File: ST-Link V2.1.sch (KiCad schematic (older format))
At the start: 3 parts

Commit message: drawing schematic
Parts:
- removed U?: stm32, symbol stm32
- added C10, C3: 1uF, symbol C
- added C15, C17, C18, C2, C5, C8, C9: 100nF, symbol C
- added C4: 10nF, symbol C
- added C6, C7: 20pF, symbol C
- added D? (x2): D, symbol D
- added J?: Conn_01x06, symbol Conn_01x06
- added LD1: LED_Dual_ACAC, symbol LED_Dual_ACAC
- added LD2: LED,RED, symbol LED
- added R1: 0, symbol R
- added R11, R2, R3: 100, symbol R
- added R14, R31: 100K, symbol R
- added R15: 4K7, symbol R
- added R16: 2K7, symbol R
- added R24: 10K, symbol R
- added R28: [NA], symbol R
- added R33, R34, R35: 22, symbol R
- added R4: 1K, symbol R
- added U2: LD3985M33R_SOT23, TO_SOT_Packages_SMD:SOT-23-5, symbol LD3985M33R_SOT23
- added U?: stm32, symbol stm32
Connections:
- net labels added: 3V3_ST_LINK, AIN_1, LED_STLINK, PWR_ENn, PWR_EXT, STLINK_RX, STM_JTCK, STM_JTMS, SWIM, SWIM_IN, SWIM_RST, SWIM_RST_IN, T_JTCK, T_JTMS, T_NRST, T_SWDIO_IN, T_SWO, USB_DM, USB_DP, USB_RENUMn, undone
- net labels removed: +3V3
- wire segments 23 -> 141
- no-connect marks 9 -> 12

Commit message: continue schematic
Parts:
- added C16: 20pF, symbol C
- added R22: 100, symbol R
- added R29, R30: 4K7, symbol R
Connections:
- net labels added: 3V3_ST_LINK1, AIN1, STLINK_TX
- wire segments 141 -> 148
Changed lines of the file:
@@
 Text GLabel 1300 2600 1    60   Input ~ 0
-undone
-Text GLabel 1800 2050 1    60   Input ~ 0
 undone
 $Comp
@@
 	800  3150 800  3600
 Wire Wire Line
-	800  3600 1750 3600
-Wire Wire Line
 	1750 3600 1750 3450
-Wire Wire Line
-	1450 3450 2600 3450
 Wire Wire Line
 	2550 3350 1450 3350
@@
 Connection ~ 1750 3450
 Connection ~ 1450 3350
-Text GLabel 1450 3300 1    60   Input ~ 0
-undone
 NoConn ~ 2550 3550
 Wire Wire Line
@@
 	7750 3900 7750 4000
 Connection ~ 8600 3900
+Wire Wire Line
+	4650 3250 5450 3250
+$Comp
+L R R22
+U 1 1 59D3403D
+P 5600 3250
+F 0 "R22" V 5680 3250 50  0000 C CNN
+F 1 "100" V 5600 3250 50  0000 C CNN
+F 2 "" V 5530 3250 50  0001 C CNN
+F 3 "" H 5600 3250 50  0001 C CNN
+	1    5600 3250
+	0    1    1    0
+$EndComp
+Wire Wire Line
+	5750 3250 6050 3250
+$Comp
+L C C16
+U 1 1 59D34298
+P 5850 3500
+F 0 "C16" H 5875 3600 50  0000 L CNN
+F 1 "20pF" H 5875 3400 50  0000 L CNN
+F 2 "" H 5888 3350 50  0001 C CNN
+F 3 "" H 5850 3500 50  0001 C CNN
+	1    5850 3500
+	1    0    0    -1
+$EndComp
+Wire Wire Line
+	5850 3250 5850 3350
+Connection ~ 5850 3250
+$Comp
+L GNDREF #PWR?
+U 1 1 59D34548
+P 5850 3650
+F 0 "#PWR?" H 5850 3400 50  0001 C CNN
+F 1 "GNDREF" H 5850 3500 50  0000 C CNN
+F 2 "" H 5850 3650 50  0001 C CNN
+F 3 "" H 5850 3650 50  0001 C CNN
+	1    5850 3650
+	1    0    0    -1
+$EndComp
+Wire Wire Line
+	950  2400 950  2500
+Text Label 950  2500 2    60   ~ 0
+3V3_ST_LINK1
+Wire Wire Line
+	1000 3550 1000 3700
+Connection ~ 1000 3600
+Wire Wire Line
+	1400 3300 1500 3300
+Text Label 1450 3300 0    60   ~ 0
+3V3_ST_LINK1
+$Comp
+L R R30
+U 1 1 59D3CD64
+P 1600 3450
+F 0 "R30" V 1680 3450 50  0000 C CNN
+F 1 "4K7" V 1600 3450 50  0000 C CNN
+F 2 "" V 1530 3450 50  0001 C CNN
+F 3 "" H 1600 3450 50  0001 C CNN
+	1    1600 3450
+	0    1    1    0
+$EndComp
+$Comp
+L R R29
+U 1 1 59D3CE9B
+P 1500 3600
+F 0 "R29" V 1580 3600 50  0000 C CNN
+F 1 "4K7" V 1500 3600 50  0000 C CNN
+F 2 "" V 1430 3600 50  0001 C CNN
+F 3 "" H 1500 3600 50  0001 C CNN
+	1    1500 3600
+	0    1    1    0
+$EndComp
+Wire Wire Line
+	1650 3600 1750 3600
+Wire Wire Line
+	800  3600 1350 3600
+Wire Wire Line
+	1750 3450 2550 3450
+Text Label 2350 3450 0    60   ~ 0
+AIN1
+Text Label 2400 4000 1    60   ~ 0
+STLINK_TX
+$Comp
+L GNDREF #PWR?
+U 1 1 59D3E32B
+P 1000 3700
+F 0 "#PWR?" H 1000 3450 50  0001 C CNN
+F 1 "GNDREF" H 1000 3550 50  0000 C CNN
+F 2 "" H 1000 3700 50  0001 C CNN
+F 3 "" H 1000 3700 50  0001 C CNN
+	1    1000 3700
+	1    0    0    -1
+$EndComp
 $EndSCHEMATC

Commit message: left usb and power part schematic
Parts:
- added J?: Conn_02x08_Row_Letter_First, symbol Conn_02x08_Row_Letter_First
- added JP2: Conn_02x01, symbol Conn_02x01
- added R13, R14: 47, symbol R
- added R8, R9: 220, symbol R
- added X1: 8MHz, symbol Crystal
- gave numbers to parts that had none: 1
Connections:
- net labels added: 5V_IN, RESET, ST_LINK_SWIM
- wire segments 148 -> 159
- no-connect marks 12 -> 14
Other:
- moved on the sheet: D?, R24, R28, R33, R34, R35

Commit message: still the same
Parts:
- added C? (x4): 1uF, symbol C
- added J?: USB_OTG, symbol USB_OTG
- added R?: R, symbol R
- added U?: MIC5219-3.3, TO_SOT_Packages_SMD:SOT-23-5, symbol MIC5219-3.3
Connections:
- wire segments 159 -> 176

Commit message: questions
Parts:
- removed D?: D, symbol D
- removed J?: Conn_01x06, symbol Conn_01x06
- removed R24: 10K, symbol R
- removed R28: [NA], symbol R
- removed R33, R34, R35: 22, symbol R
- added R10: 100, symbol R
- added R23: 36K, symbol R
- added R5: 100K, symbol R
- added R7, R8: 20, symbol R
- added R9: 10K, symbol R
- R6: renamed from R?; value R -> 1K5
- gave numbers to parts that had none: 8
- renumbered R14 to R19, R8 to R20, R9 to R21
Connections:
- net labels added: USB_RENUMN
- net labels removed: 3V3_ST_LINK1, AIN_1, T_JTMS, undone
- wire segments 176 -> 167
- no-connect marks 14 -> 13
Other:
- moved on the sheet: C15, C17, C5, C8, LD1, LD2, R1, R15, R2, R3, R4

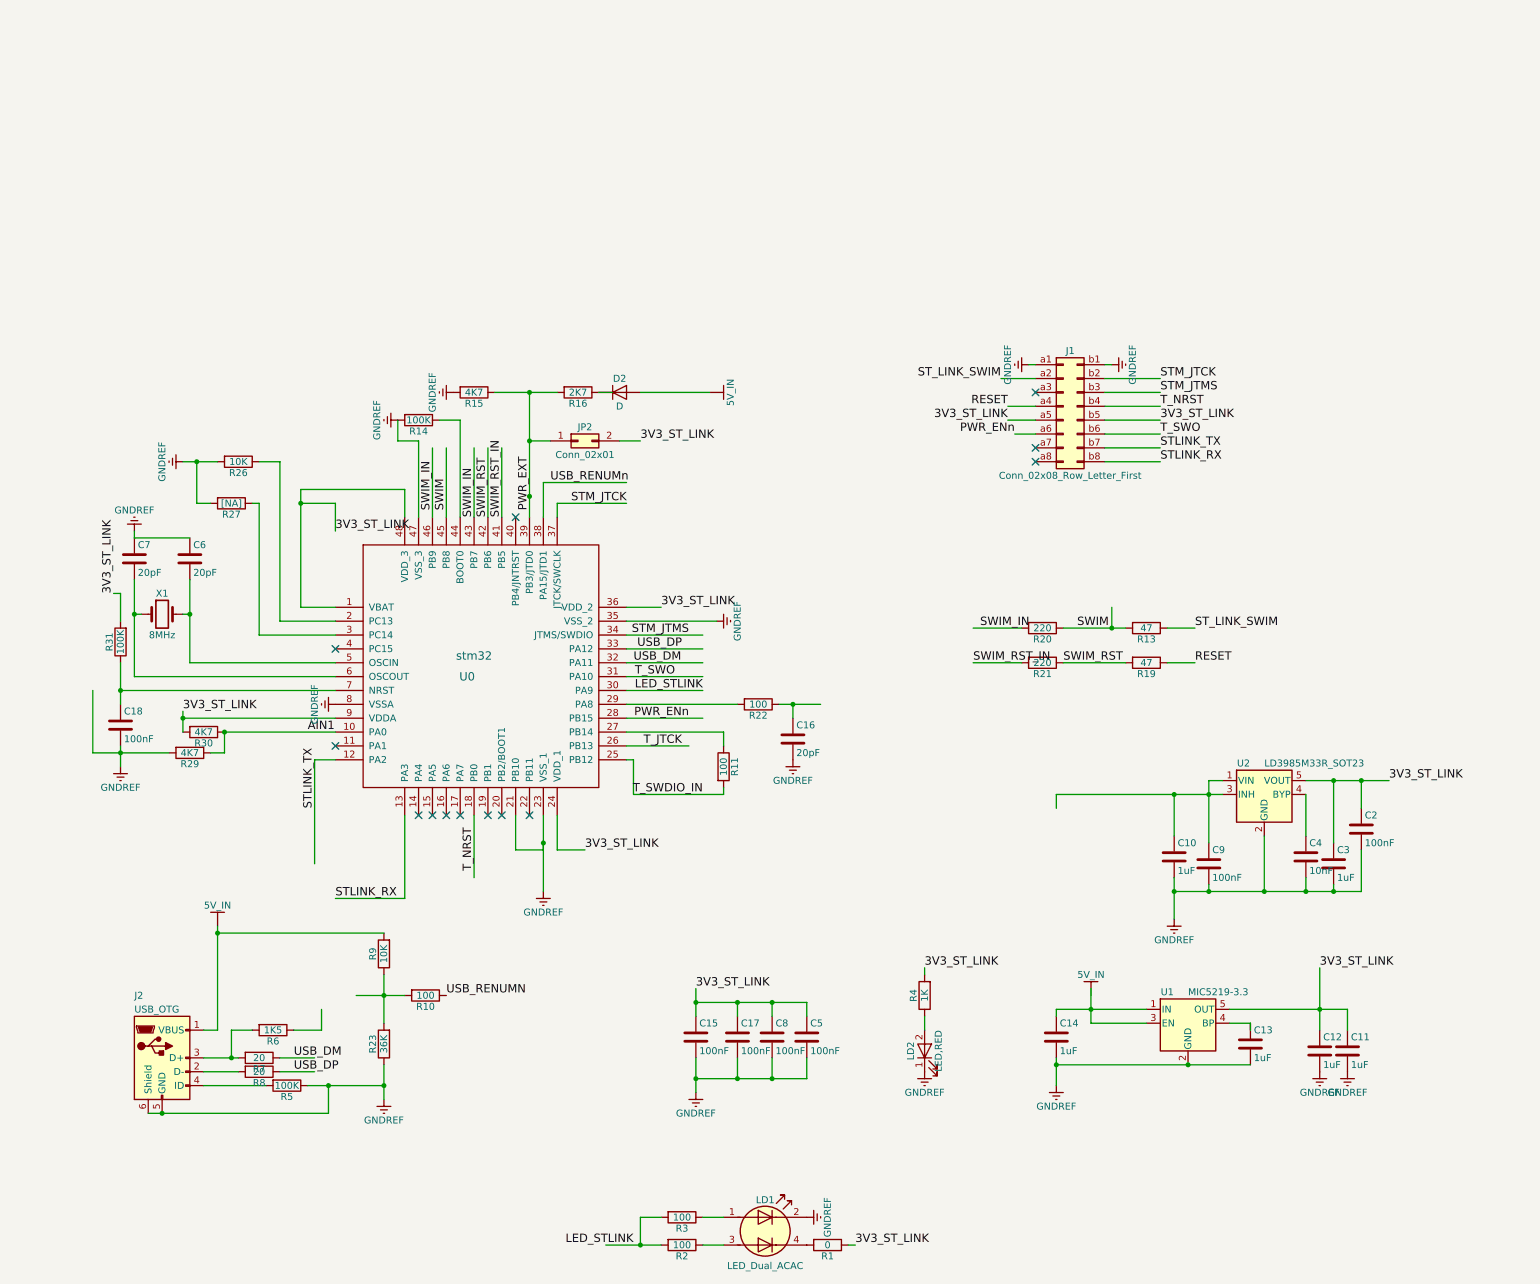
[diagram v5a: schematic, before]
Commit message: can start footprint
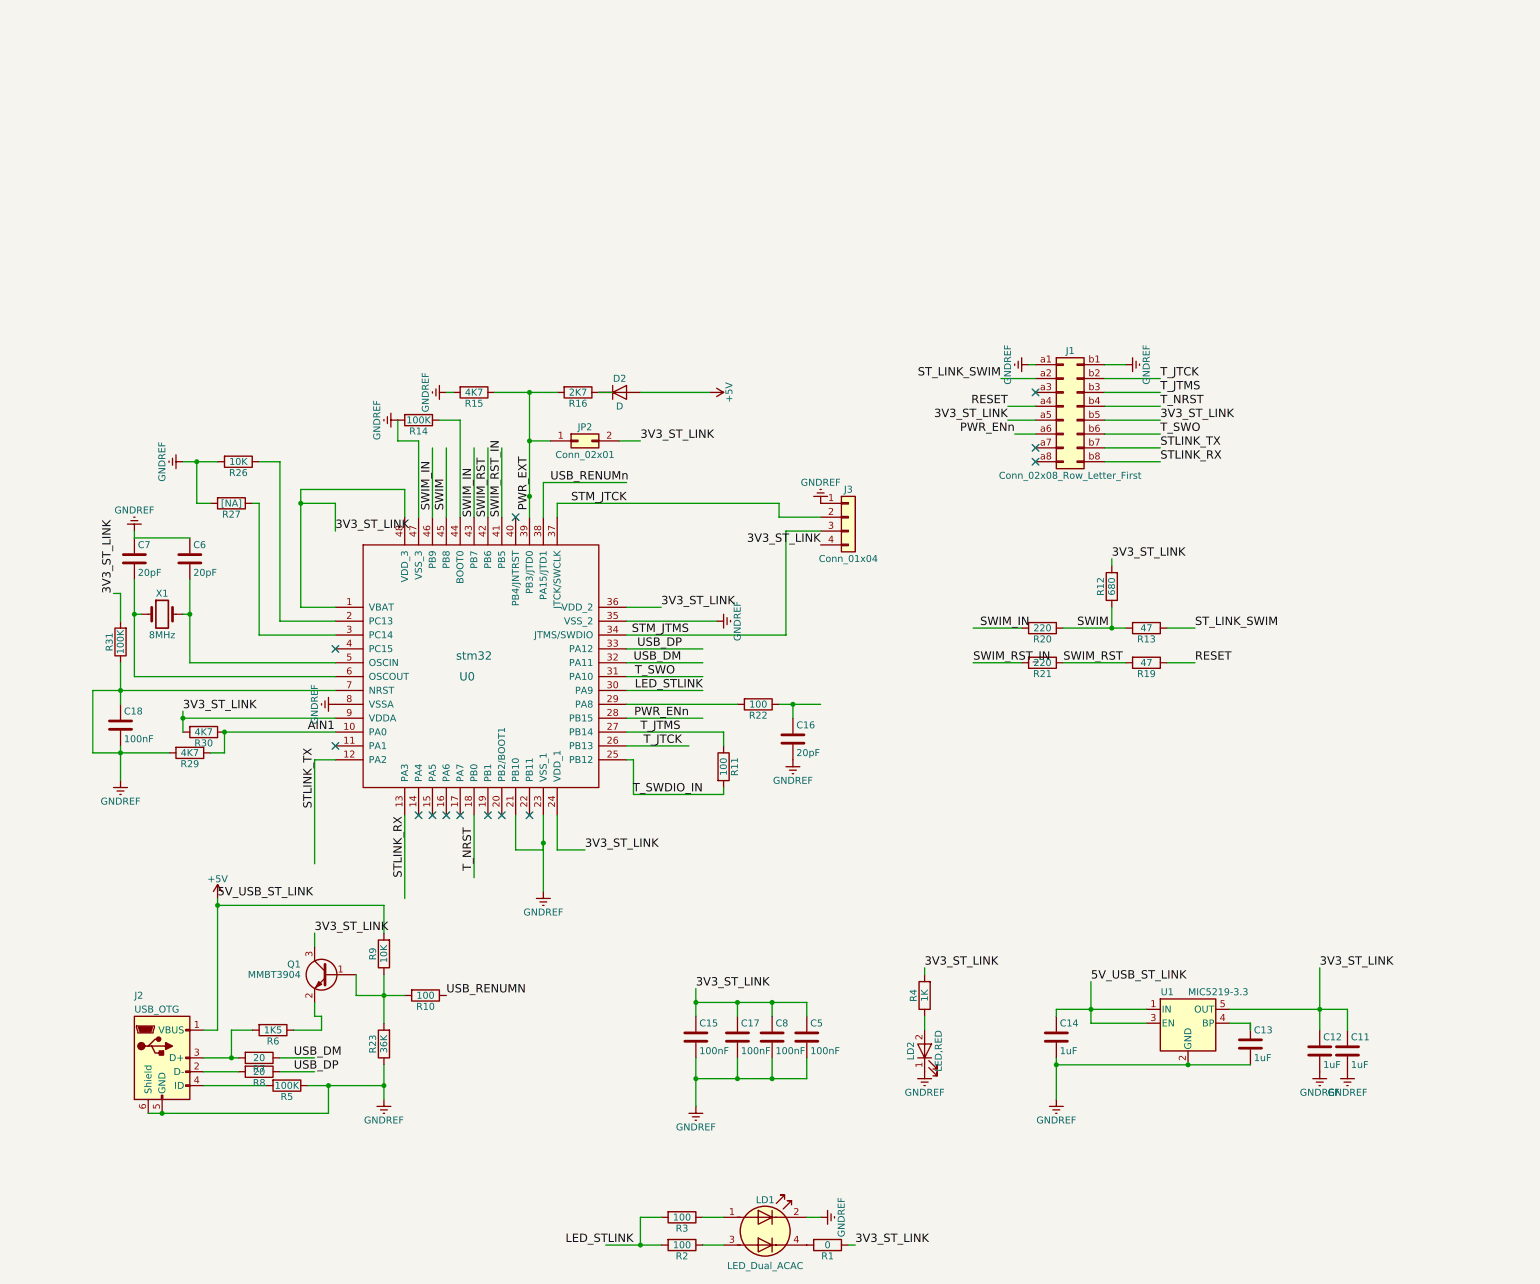
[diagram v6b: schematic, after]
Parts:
- removed C10, C3: 1uF, symbol C
- removed C2, C9: 100nF, symbol C
- removed C4: 10nF, symbol C
- removed U2: LD3985M33R_SOT23, TO_SOT_Packages_SMD:SOT-23-5, symbol LD3985M33R_SOT23
- added J3: Conn_01x04, symbol Conn_01x04
- added Q1: MMBT3904, TO_SOT_Packages_SMD:SOT-23, symbol MMBT3904
- added R12: 680, symbol R
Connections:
- net labels added: +5V, 5V_USB_ST_LINK, T_JTMS
- net labels removed: 5V_IN
- wire segments 167 -> 162

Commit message: 01
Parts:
- removed J1: Conn_02x08_Row_Letter_First, symbol Conn_02x08_Row_Letter_First
- removed J3: Conn_01x04, symbol Conn_01x04
- added J1, J4: Conn_01x08, symbol Conn_01x08
- added J3: Conn_01x05, symbol Conn_01x05
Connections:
- net labels added: MCO, T_JRST
- wire segments 162 -> 159
- no-connect marks 13 -> 12
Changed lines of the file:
@@
 NoConn ~ 3950 4050
 NoConn ~ 3750 4050
-NoConn ~ 3650 4050
 NoConn ~ 3450 4050
 NoConn ~ 3350 4050
@@
 Text Label 5050 3550 2    60   ~ 0
 T_JTCK
-Text Label 4250 1800 0    60   ~ 0
+Text Label 4150 1800 0    60   ~ 0
 STM_JTCK
 Text Label 4100 1650 0    60   ~ 0
@@
 $EndComp
 $Comp
-L Conn_02x08_Row_Letter_First J1
-U 1 1 59D5C481
-P 7800 1100
-F 0 "J1" H 7850 1500 50  0000 C CNN
-F 1 "Conn_02x08_Row_Letter_First" H 7850 600 50  0000 C CNN
-F 2 "" H 7800 1100 50  0001 C CNN
-F 3 "" H 7800 1100 50  0001 C CNN
-	1    7800 1100
-	1    0    0    -1
-$EndComp
-$Comp
 L GNDREF #PWR012
 U 1 1 59D5F43A
-P 7550 800
-F 0 "#PWR012" H 7550 550 50  0001 C CNN
-F 1 "GNDREF" H 7550 650 50  0000 C CNN
-F 2 "" H 7550 800 50  0001 C CNN
-F 3 "" H 7550 800 50  0001 C CNN
-	1    7550 800
+P 9200 800
+F 0 "#PWR012" H 9200 550 50  0001 C CNN
+F 1 "GNDREF" H 9200 650 50  0000 C CNN
+F 2 "" H 9200 800 50  0001 C CNN
+F 3 "" H 9200 800 50  0001 C CNN
+	1    9200 800
 	0    1    1    0
 $EndComp
@@
 L GNDREF #PWR013
 U 1 1 59D61FA6
-P 8250 800
-F 0 "#PWR013" H 8250 550 50  0001 C CNN
-F 1 "GNDREF" H 8250 650 50  0000 C CNN
-F 2 "" H 8250 800 50  0001 C CNN
-F 3 "" H 8250 800 50  0001 C CNN
-	1    8250 800
+P 10250 800
+F 0 "#PWR013" H 10250 550 50  0001 C CNN
+F 1 "GNDREF" H 10250 650 50  0000 C CNN
+F 2 "" H 10250 800 50  0001 C CNN
+F 3 "" H 10250 800 50  0001 C CNN
+	1    10250 800
 	0    -1   -1   0
 $EndComp
 Text Label 3550 4450 1    60   ~ 0
 T_NRST
-Text Label 8500 1100 0    60   ~ 0
+Text Label 10500 1100 0    60   ~ 0
 T_NRST
-Text Label 8500 1300 0    60   ~ 0
+Text Label 10500 1300 0    60   ~ 0
 T_SWO
-Text Label 8500 1400 0    60   ~ 0
+Text Label 10500 1400 0    60   ~ 0
 STLINK_TX
-Text Label 8500 1500 0    60   ~ 0
+Text Label 10500 1500 0    60   ~ 0
 STLINK_RX
 $Comp
@@
 Text Label 8750 2950 0    60   ~ 0
 RESET
-Text Label 7350 900  2    60   ~ 0
+Text Label 9000 900  2    60   ~ 0
 ST_LINK_SWIM
-NoConn ~ 7600 1000
-NoConn ~ 7600 1500
-NoConn ~ 7600 1400
-Text Label 7400 1100 2    60   ~ 0
+Text Label 9050 1100 2    60   ~ 0
 RESET
-Text Label 7450 1300 2    60   ~ 0
+Text Label 9100 1300 2    60   ~ 0
 PWR_ENn
 $Comp
@@
 	0    1    1    0
 $EndComp
-Text Label 2250 5800 0    60   ~ 0
+Text Label 2400 5900 0    60   ~ 0
 USB_DM
-Text Label 2250 5900 0    60   ~ 0
+Text Label 2400 5800 0    60   ~ 0
 USB_DP
 $Comp
@@
 Text Label 9650 5150 0    60   ~ 0
 3V3_ST_LINK
-Text Label 8500 1200 0    60   ~ 0
-3V3_ST_LINK
-Text Label 7400 1200 2    60   ~ 0
+Text Label 10500 1200 0    60   ~ 0
+3V3_ST_LINK
+Text Label 9050 1200 2    60   ~ 0
 3V3_ST_LINK
 Text Label 4750 1350 0    60   ~ 0
@@
 	6800 5150 6800 5200
 Wire Wire Line
-	7400 1200 7600 1200
-Wire Wire Line
-	8100 1200 8500 1200
+	9050 1200 9250 1200
+Wire Wire Line
+	10100 1200 10500 1200
 Wire Wire Line
 	4650 2550 4900 2550
@@
 	2400 3650 2400 4400
 Wire Wire Line
-	7600 1300 7450 1300
-Wire Wire Line
-	7600 1100 7400 1100
-Wire Wire Line
-	7600 900  7350 900
+	9250 1300 9100 1300
+Wire Wire Line
+	9250 1100 9050 1100
+Wire Wire Line
+	9250 900  9000 900
 Wire Wire Line
 	8550 2950 8750 2950
@@
 	7150 2700 7500 2700
 Wire Wire Line
-	8100 1500 8500 1500
-Wire Wire Line
-	8100 1400 8500 1400
-Wire Wire Line
-	8100 1300 8500 1300
-Wire Wire Line
-	8100 1000 8500 1000
-Wire Wire Line
-	8100 1100 8500 1100
-Wire Wire Line
-	8100 900  8500 900
+	10100 1500 10500 1500
+Wire Wire Line
+	10100 1400 10500 1400
+Wire Wire Line
+	10100 1300 10500 1300
+Wire Wire Line
+	10100 1000 10500 1000
+Wire Wire Line
+	10100 1100 10500 1100
+Wire Wire Line
+	10100 900  10500 900
 Wire Wire Line
 	3550 4050 3550 4500
 Wire Wire Line
-	8100 800  8250 800
-Wire Wire Line
-	7550 800  7600 800
+	10100 800  10250 800
+Wire Wire Line
+	9200 800  9250 800
 Wire Wire Line
 	1500 2950 2550 2950
@@
 Wire Wire Line
 	4050 1900 4050 1650
-Wire Wire Line
-	4150 1800 5750 1800
 Wire Wire Line
 	4150 1900 4150 1800
@@
 	1    0    0    -1
 $EndComp
-Text Label 8500 900  0    60   ~ 0
+Text Label 10500 900  0    60   ~ 0
 T_JTCK
 Text Label 4750 3450 0    60   ~ 0
 T_JTMS
-Text Label 8500 1000 0    60   ~ 0
+Text Label 10500 1000 0    60   ~ 0
 T_JTMS
-$Comp
-L Conn_01x04 J3
-U 1 1 59DBE2C0
-P 6250 1900
-F 0 "J3" H 6250 2100 50  0000 C CNN
-F 1 "Conn_01x04" H 6250 1600 50  0000 C CNN
-F 2 "" H 6250 1900 50  0001 C CNN
-F 3 "" H 6250 1900 50  0001 C CNN
-	1    6250 1900
-	1    0    0    -1
-$EndComp
-Wire Wire Line
-	5800 2750 5800 2000
-Wire Wire Line
-	5800 2000 6050 2000
-Wire Wire Line
-	5750 1800 5750 1900
-Wire Wire Line
-	5750 1900 6050 1900
 $Comp
 L GNDREF #PWR021
@@
 	-1   0    0    1
 $EndComp
-Text Label 6050 2100 2    60   ~ 0
-3V3_ST_LINK
+Text Label 6500 2200 2    60   ~ 0
+3V3_ST_LINK
+$Comp
+L Conn_01x05 J3
+U 1 1 59D6FF42
+P 6700 2000
+F 0 "J3" H 6700 2300 50  0000 C CNN
+F 1 "Conn_01x05" H 6700 1700 50  0000 C CNN
+F 2 "" H 6700 2000 50  0001 C CNN
+F 3 "" H 6700 2000 50  0001 C CNN
+	1    6700 2000
+	1    0    0    -1
+$EndComp
+Wire Wire Line
+	6050 1800 6500 1800
+Text Label 6500 1900 2    60   ~ 0
+STM_JTCK
+Text Label 6500 2000 2    60   ~ 0
+STM_JTMS
+Wire Wire Line
+	3650 4050 3650 4500
+Text Label 3650 4450 1    60   ~ 0
+T_JRST
+Text Label 6500 2100 2    60   ~ 0
+T_JRST
+$Comp
+L Conn_01x08 J1
+U 1 1 59D7D629
+P 9450 1100
+F 0 "J1" H 9450 1500 50  0000 C CNN
+F 1 "Conn_01x08" H 9450 600 50  0000 C CNN
+F 2 "" H 9450 1100 50  0001 C CNN
+F 3 "" H 9450 1100 50  0001 C CNN
+	1    9450 1100
+	1    0    0    -1
+$EndComp
+$Comp
+L Conn_01x08 J4
+U 1 1 59D7D6EA
+P 9900 1100
+F 0 "J4" H 9900 1500 50  0000 C CNN
+F 1 "Conn_01x08" H 9900 600 50  0000 C CNN
+F 2 "" H 9900 1100 50  0001 C CNN
+F 3 "" H 9900 1100 50  0001 C CNN
+	1    9900 1100
+	-1   0    0    -1
+$EndComp
+NoConn ~ 9250 1000
+NoConn ~ 9250 1400
+NoConn ~ 9250 1500
+Text Label 6050 3250 0    60   ~ 0
+MCO
 $EndSCHEMATC

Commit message: ALLIGNING
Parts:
- removed D2: D, symbol D
- removed J3: Conn_01x05, symbol Conn_01x05
- removed JP2: Conn_02x01, symbol Conn_02x01
- removed LD1: LED_Dual_ACAC, symbol LED_Dual_ACAC
- removed R16: 2K7, symbol R
- added D1, D2: LED, LEDs:LED_0603, symbol LED
- added U2: USBLC6-2SC6, symbol USBLC6-2SC6
- C11, C12, C13, C14, C15, C16, C17, C18, C5, C6, C7, C8: footprint (none) -> Capacitors_SMD:C_0603
- J1, J4: footprint (none) -> Socket_Strips:Socket_Strip_Angled_1x08_Pitch2.54mm
- J2: footprint (none) -> Connectors_USB:USB_Micro-B_Molex-105017-0001
- LD2: footprint (none) -> LEDs:LED_0603
- R1, R10, R11, R12, R13, R14, R19, R20, R21, R22, R23, R26, R27, R29, R30, R31, R4, R5, R6, R7, R8, R9: footprint (none) -> Resistors_SMD:R_0603_HandSoldering
- R15: value 4K7 -> 4.7K; footprint (none) -> Resistors_SMD:R_0603_HandSoldering
- R2, R3: value 100 -> 220; footprint (none) -> Resistors_SMD:R_0603_HandSoldering
- U0: footprint (none) -> UFQFPN48:UFQFPN48
- X1: footprint (none) -> Crystals:Crystal_HC49-4H_Vertical
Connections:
- net labels added: NRST
- net labels removed: PWR_EXT, T_JRST
- wire segments 159 -> 161
- no-connect marks 12 -> 16
